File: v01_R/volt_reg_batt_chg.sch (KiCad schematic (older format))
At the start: 13 parts, among them P13 JST-PH2, Q3 PNP, SW3 DIPS_01, U4 MIC5219

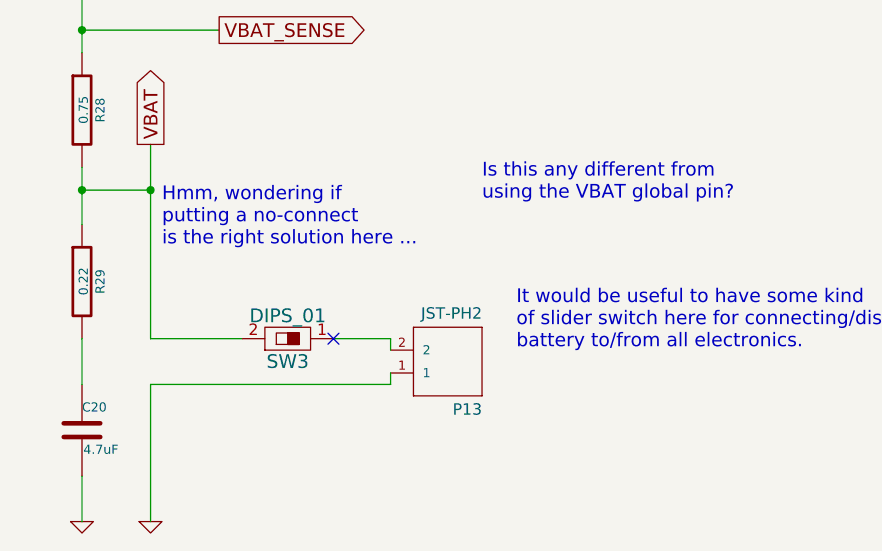
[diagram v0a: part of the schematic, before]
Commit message: Update removes the left channel of the audio circuit.
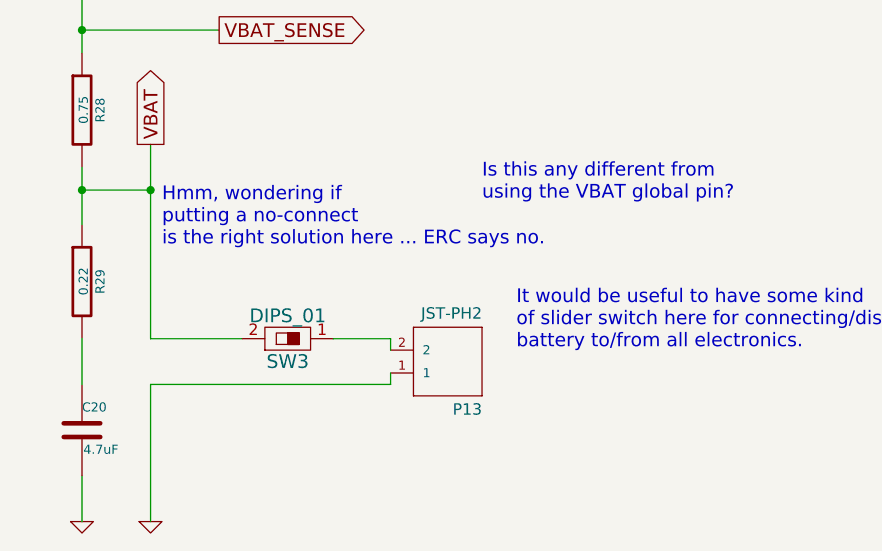
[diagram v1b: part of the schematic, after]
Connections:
- no-connect marks 2 -> 1
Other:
- note added: "Hmm, wondering if \nputting a no-connect\nis the right solution here ... ERC says no."
- note removed: "Hmm, wondering if \nputting a no-connect\nis the right solution here ..."
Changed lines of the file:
@@
 Sheet 4 4
 Title ""
-Date "7 dec 2014"
+Date "16 jan 2015"
 Rev ""
 Comp ""
@@
 $EndComp
 $Comp
-L GND #PWR18
+L GND #PWR013
 U 1 1 5439B1A3
 P 4900 2700
-F 0 "#PWR18" H 4900 2700 30  0001 C CNN
+F 0 "#PWR013" H 4900 2700 30  0001 C CNN
 F 1 "GND" H 4900 2630 30  0001 C CNN
 F 2 "" H 4900 2700 60  0000 C CNN
@@
 $EndComp
 $Comp
-L GND #PWR15
+L GND #PWR014
 U 1 1 5439B578
 P 2250 6250
-F 0 "#PWR15" H 2250 6250 30  0001 C CNN
+F 0 "#PWR014" H 2250 6250 30  0001 C CNN
 F 1 "GND" H 2250 6180 30  0001 C CNN
 F 2 "" H 2250 6250 60  0000 C CNN
@@
 3.3V
 $Comp
-L PWR_FLAG #FLG2
+L PWR_FLAG #FLG015
 U 1 1 5439CBDC
 P 2150 1600
-F 0 "#FLG2" H 2150 1695 30  0001 C CNN
+F 0 "#FLG015" H 2150 1695 30  0001 C CNN
 F 1 "PWR_FLAG" H 2150 1780 30  0000 C CNN
 F 2 "" H 2150 1600 60  0000 C CNN
@@
 $EndComp
 $Comp
-L +BATT #PWR14
+L +BATT #PWR016
 U 1 1 5439CC42
 P 2150 1850
-F 0 "#PWR14" H 2150 1800 20  0001 C CNN
+F 0 "#PWR016" H 2150 1800 20  0001 C CNN
 F 1 "+BATT" H 2150 1950 30  0000 C CNN
 F 2 "" H 2150 1850 60  0000 C CNN
@@
 VIN
 $Comp
-L GND #PWR17
+L GND #PWR017
 U 1 1 5439D063
 P 2550 6250
-F 0 "#PWR17" H 2550 6250 30  0001 C CNN
+F 0 "#PWR017" H 2550 6250 30  0001 C CNN
 F 1 "GND" H 2550 6180 30  0001 C CNN
 F 2 "" H 2550 6250 60  0000 C CNN
@@
 	1850 1600 1850 1850
 $Comp
-L +5V #PWR13
+L +5V #PWR018
 U 1 1 5439CBF7
 P 1850 1850
-F 0 "#PWR13" H 1850 1940 20  0001 C CNN
+F 0 "#PWR018" H 1850 1940 20  0001 C CNN
 F 1 "+5V" H 1850 1940 30  0000 C CNN
 F 2 "" H 1850 1850 60  0000 C CNN
@@
 $EndComp
 $Comp
-L PWR_FLAG #FLG1
+L PWR_FLAG #FLG019
 U 1 1 5439CBEF
 P 1850 1600
-F 0 "#FLG1" H 1850 1695 30  0001 C CNN
+F 0 "#FLG019" H 1850 1695 30  0001 C CNN
 F 1 "PWR_FLAG" H 1850 1780 30  0000 C CNN
 F 2 "" H 1850 1600 60  0000 C CNN
@@
 	2450 1600 2450 1900
 $Comp
-L GND #PWR16
+L GND #PWR020
 U 1 1 5439CC8E
 P 2450 1900
-F 0 "#PWR16" H 2450 1900 30  0001 C CNN
+F 0 "#PWR020" H 2450 1900 30  0001 C CNN
 F 1 "GND" H 2450 1830 30  0001 C CNN
 F 2 "" H 2450 1900 60  0000 C CNN
@@
 $EndComp
 $Comp
-L PWR_FLAG #FLG3
+L PWR_FLAG #FLG021
 U 1 1 5439CBE9
 P 2450 1600
-F 0 "#FLG3" H 2450 1695 30  0001 C CNN
+F 0 "#FLG021" H 2450 1695 30  0001 C CNN
 F 1 "PWR_FLAG" H 2450 1780 30  0000 C CNN
 F 2 "" H 2450 1600 60  0000 C CNN
@@
 	0    -1   -1   0
 $EndComp
-NoConn ~ 3350 5450
 Text Notes 2600 5050 0    60   ~ 0
-Hmm, wondering if \nputting a no-connect\nis the right solution here ...
+Hmm, wondering if \nputting a no-connect\nis the right solution here ... ERC says no.
 $Comp
 L JST-PH2 P13

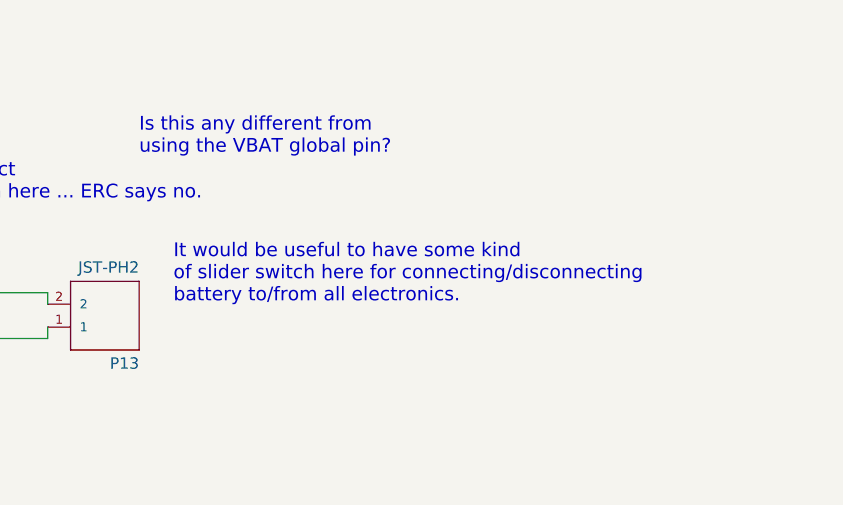
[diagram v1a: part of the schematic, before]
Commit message: Updating entire schematic and footprint selections. Adding jst-ph footprints.
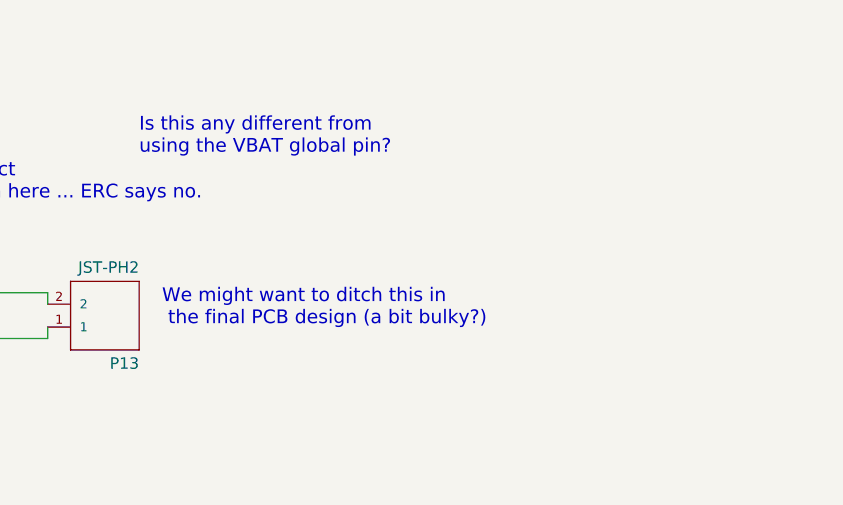
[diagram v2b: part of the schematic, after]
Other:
- note added: "We might want to ditch this in\n the final PCB design (a bit bulky?)"
- note removed: "It would be useful to have some kind \nof slider switch here for connecting/disconnecting \nbattery to/from all electronics."
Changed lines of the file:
@@
 Sheet 4 4
 Title ""
-Date "16 jan 2015"
+Date "17 jan 2015"
 Rev ""
 Comp ""
@@
 $EndComp
 $Comp
-L GND #PWR013
+L GND #PWR012
 U 1 1 5439B1A3
 P 4900 2700
-F 0 "#PWR013" H 4900 2700 30  0001 C CNN
+F 0 "#PWR012" H 4900 2700 30  0001 C CNN
 F 1 "GND" H 4900 2630 30  0001 C CNN
 F 2 "" H 4900 2700 60  0000 C CNN
@@
 $EndComp
 $Comp
-L GND #PWR014
+L GND #PWR013
 U 1 1 5439B578
 P 2250 6250
-F 0 "#PWR014" H 2250 6250 30  0001 C CNN
+F 0 "#PWR013" H 2250 6250 30  0001 C CNN
 F 1 "GND" H 2250 6180 30  0001 C CNN
 F 2 "" H 2250 6250 60  0000 C CNN
@@
 3.3V
 $Comp
-L PWR_FLAG #FLG015
+L PWR_FLAG #FLG014
 U 1 1 5439CBDC
 P 2150 1600
-F 0 "#FLG015" H 2150 1695 30  0001 C CNN
+F 0 "#FLG014" H 2150 1695 30  0001 C CNN
 F 1 "PWR_FLAG" H 2150 1780 30  0000 C CNN
 F 2 "" H 2150 1600 60  0000 C CNN
@@
 $EndComp
 $Comp
-L +BATT #PWR016
+L +BATT #PWR015
 U 1 1 5439CC42
 P 2150 1850
-F 0 "#PWR016" H 2150 1800 20  0001 C CNN
+F 0 "#PWR015" H 2150 1800 20  0001 C CNN
 F 1 "+BATT" H 2150 1950 30  0000 C CNN
 F 2 "" H 2150 1850 60  0000 C CNN
@@
 VIN
 $Comp
-L GND #PWR017
+L GND #PWR016
 U 1 1 5439D063
 P 2550 6250
-F 0 "#PWR017" H 2550 6250 30  0001 C CNN
+F 0 "#PWR016" H 2550 6250 30  0001 C CNN
 F 1 "GND" H 2550 6180 30  0001 C CNN
 F 2 "" H 2550 6250 60  0000 C CNN
@@
 Wire Wire Line
 	1550 3500 1350 3500
-Text Notes 4150 5500 0    60   ~ 0
-It would be useful to have some kind \nof slider switch here for connecting/disconnecting \nbattery to/from all electronics.
+Text Notes 4100 5600 0    60   ~ 0
+We might want to ditch this in\n the final PCB design (a bit bulky?)
 Text Notes 1300 2200 0    60   ~ 0
 I wonder if you need\nthis on all of the sheets ... No.
@@
 	1850 1600 1850 1850
 $Comp
-L +5V #PWR018
+L +5V #PWR017
 U 1 1 5439CBF7
 P 1850 1850
-F 0 "#PWR018" H 1850 1940 20  0001 C CNN
+F 0 "#PWR017" H 1850 1940 20  0001 C CNN
 F 1 "+5V" H 1850 1940 30  0000 C CNN
 F 2 "" H 1850 1850 60  0000 C CNN
@@
 $EndComp
 $Comp
-L PWR_FLAG #FLG019
+L PWR_FLAG #FLG018
 U 1 1 5439CBEF
 P 1850 1600
-F 0 "#FLG019" H 1850 1695 30  0001 C CNN
+F 0 "#FLG018" H 1850 1695 30  0001 C CNN
 F 1 "PWR_FLAG" H 1850 1780 30  0000 C CNN
 F 2 "" H 1850 1600 60  0000 C CNN
@@
 	2450 1600 2450 1900
 $Comp
-L GND #PWR020
+L GND #PWR019
 U 1 1 5439CC8E
 P 2450 1900
-F 0 "#PWR020" H 2450 1900 30  0001 C CNN
+F 0 "#PWR019" H 2450 1900 30  0001 C CNN
 F 1 "GND" H 2450 1830 30  0001 C CNN
 F 2 "" H 2450 1900 60  0000 C CNN
@@
 $EndComp
 $Comp
-L PWR_FLAG #FLG021
+L PWR_FLAG #FLG020
 U 1 1 5439CBE9
 P 2450 1600
-F 0 "#FLG021" H 2450 1695 30  0001 C CNN
+F 0 "#FLG020" H 2450 1695 30  0001 C CNN
 F 1 "PWR_FLAG" H 2450 1780 30  0000 C CNN
 F 2 "" H 2450 1600 60  0000 C CNN

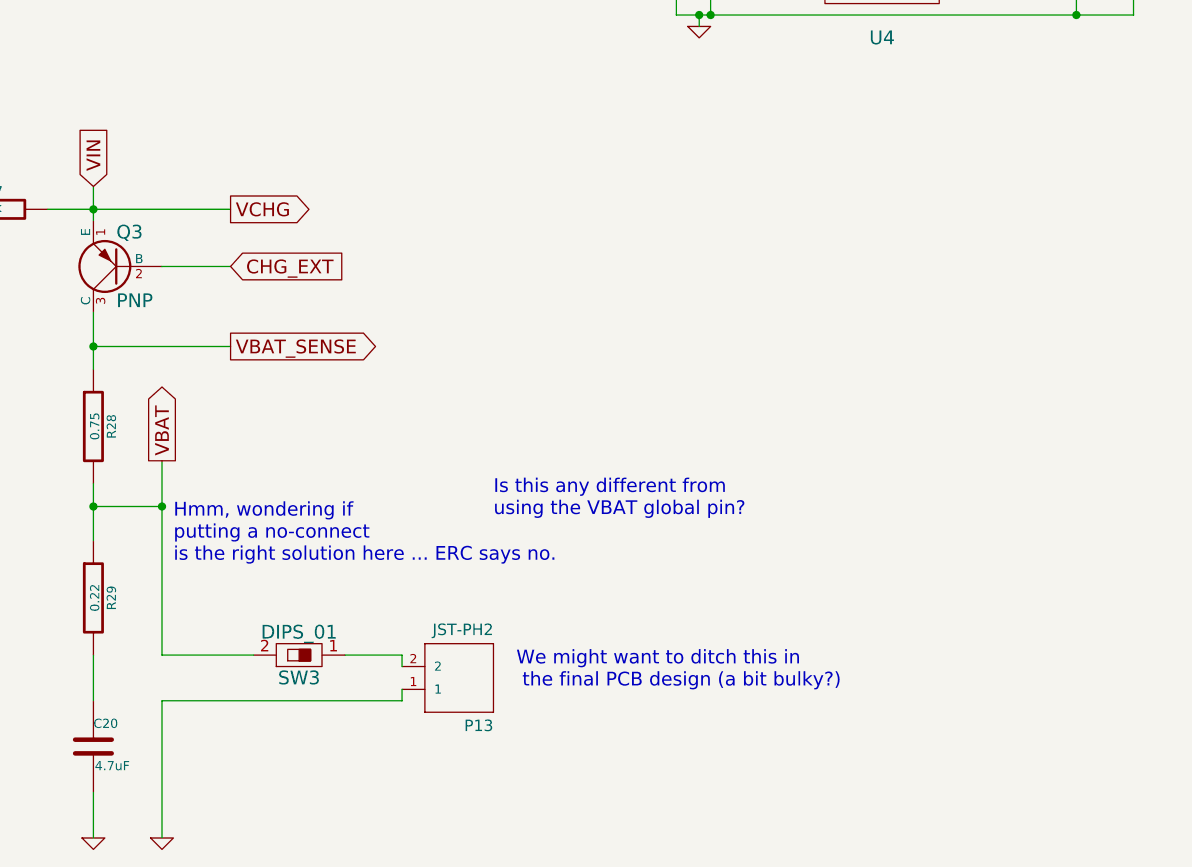
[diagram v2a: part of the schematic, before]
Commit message: Adding very rough initial version of PCB. The BA driver pads were not exact yet (based off of a Sonion driver datasheet).
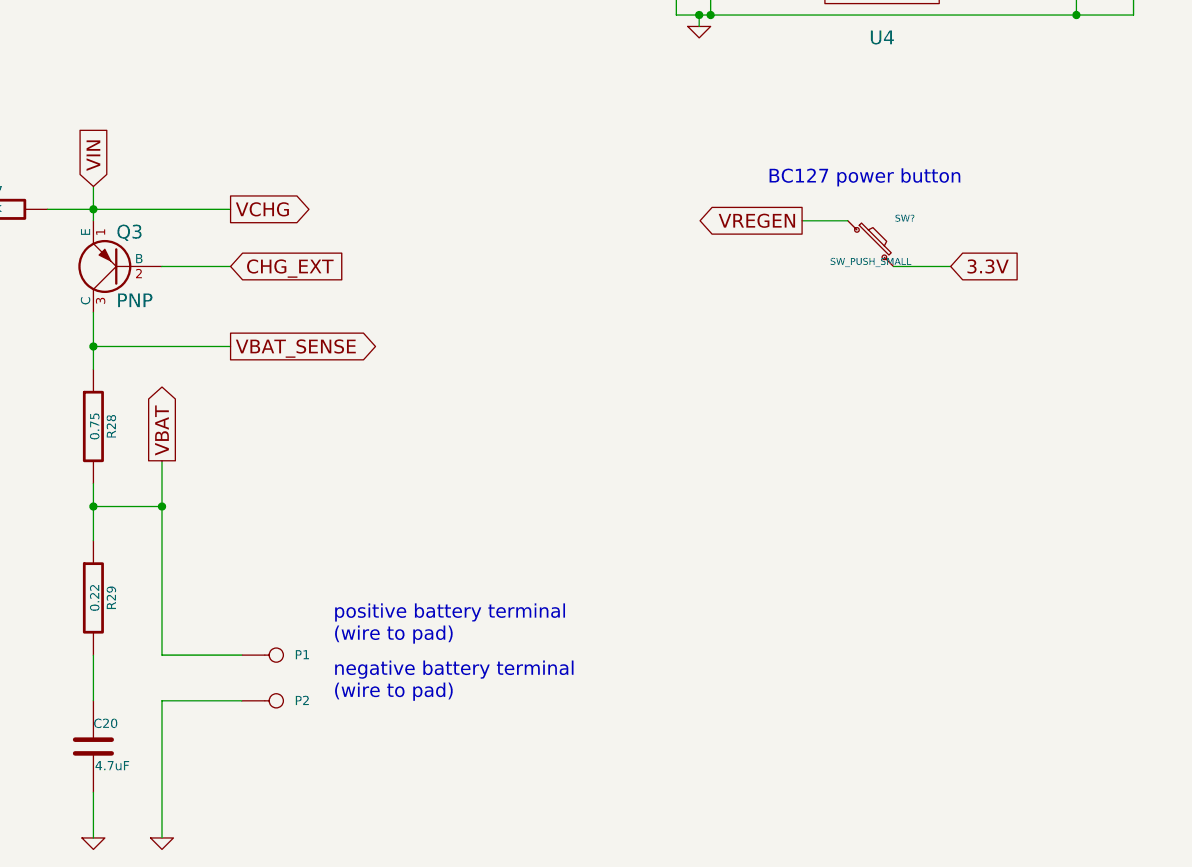
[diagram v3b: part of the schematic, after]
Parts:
- removed P13: JST-PH2, jst-ph-JST-PH2, symbol JST-PH2
- removed SW3: DIPS_01, symbol DIPS_01
- added P1, P2: CONN_1, ~, symbol CONN_1
- added SW?: SW_PUSH_SMALL, ~, symbol SW_PUSH_SMALL
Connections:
- net 3.3V: now also SW?.2
- net GND: now also P2.1
- net VBAT: now also P1.1
- new net VREGEN: SW?.1
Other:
- note added: "BC127 power button"
- note added: "negative battery terminal\n(wire to pad)"
- note added: "positive battery terminal\n(wire to pad)"
- note removed: "Hmm, wondering if \nputting a no-connect\nis the right solution here ... ERC says no."
- note removed: "Is this any different from \nusing the VBAT global pin?"
- note removed: "We might want to ditch this in\n the final PCB design (a bit bulky?)"
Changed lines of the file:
@@
 Sheet 4 4
 Title ""
-Date "17 jan 2015"
+Date "18 jan 2015"
 Rev ""
 Comp ""
@@
 $EndComp
 $Comp
-L GND #PWR012
+L GND #PWR011
 U 1 1 5439B1A3
 P 4900 2700
-F 0 "#PWR012" H 4900 2700 30  0001 C CNN
+F 0 "#PWR011" H 4900 2700 30  0001 C CNN
 F 1 "GND" H 4900 2630 30  0001 C CNN
 F 2 "" H 4900 2700 60  0000 C CNN
@@
 $EndComp
 $Comp
-L GND #PWR013
+L GND #PWR012
 U 1 1 5439B578
 P 2250 6250
-F 0 "#PWR013" H 2250 6250 30  0001 C CNN
+F 0 "#PWR012" H 2250 6250 30  0001 C CNN
 F 1 "GND" H 2250 6180 30  0001 C CNN
 F 2 "" H 2250 6250 60  0000 C CNN
@@
 3.3V
 $Comp
-L PWR_FLAG #FLG014
+L PWR_FLAG #FLG013
 U 1 1 5439CBDC
 P 2150 1600
-F 0 "#FLG014" H 2150 1695 30  0001 C CNN
+F 0 "#FLG013" H 2150 1695 30  0001 C CNN
 F 1 "PWR_FLAG" H 2150 1780 30  0000 C CNN
 F 2 "" H 2150 1600 60  0000 C CNN
@@
 $EndComp
 $Comp
-L +BATT #PWR015
+L +BATT #PWR014
 U 1 1 5439CC42
 P 2150 1850
-F 0 "#PWR015" H 2150 1800 20  0001 C CNN
+F 0 "#PWR014" H 2150 1800 20  0001 C CNN
 F 1 "+BATT" H 2150 1950 30  0000 C CNN
 F 2 "" H 2150 1850 60  0000 C CNN
@@
 VIN
 $Comp
-L GND #PWR016
+L GND #PWR015
 U 1 1 5439D063
 P 2550 6250
-F 0 "#PWR016" H 2550 6250 30  0001 C CNN
+F 0 "#PWR015" H 2550 6250 30  0001 C CNN
 F 1 "GND" H 2550 6180 30  0001 C CNN
 F 2 "" H 2550 6250 60  0000 C CNN
@@
 	2250 3400 2250 3550
 Wire Wire Line
-	3350 5450 3600 5450
+	2550 5450 2900 5450
 Wire Wire Line
 	2550 4600 2550 5450
@@
 Connection ~ 2250 4800
 Wire Wire Line
-	2550 5650 3600 5650
+	2550 5650 2900 5650
 Wire Wire Line
 	2550 5650 2550 6250
@@
 Wire Wire Line
 	1550 3500 1350 3500
-Text Notes 4100 5600 0    60   ~ 0
-We might want to ditch this in\n the final PCB design (a bit bulky?)
 Text Notes 1300 2200 0    60   ~ 0
 I wonder if you need\nthis on all of the sheets ... No.
-Text Notes 4000 4850 0    60   ~ 0
-Is this any different from \nusing the VBAT global pin?
 Wire Wire Line
 	1850 1600 1850 1850
 $Comp
-L +5V #PWR017
+L +5V #PWR016
 U 1 1 5439CBF7
 P 1850 1850
-F 0 "#PWR017" H 1850 1940 20  0001 C CNN
+F 0 "#PWR016" H 1850 1940 20  0001 C CNN
 F 1 "+5V" H 1850 1940 30  0000 C CNN
 F 2 "" H 1850 1850 60  0000 C CNN
@@
 $EndComp
 $Comp
-L PWR_FLAG #FLG018
+L PWR_FLAG #FLG017
 U 1 1 5439CBEF
 P 1850 1600
-F 0 "#FLG018" H 1850 1695 30  0001 C CNN
+F 0 "#FLG017" H 1850 1695 30  0001 C CNN
 F 1 "PWR_FLAG" H 1850 1780 30  0000 C CNN
 F 2 "" H 1850 1600 60  0000 C CNN
@@
 	2450 1600 2450 1900
 $Comp
-L GND #PWR019
+L GND #PWR018
 U 1 1 5439CC8E
 P 2450 1900
-F 0 "#PWR019" H 2450 1900 30  0001 C CNN
+F 0 "#PWR018" H 2450 1900 30  0001 C CNN
 F 1 "GND" H 2450 1830 30  0001 C CNN
 F 2 "" H 2450 1900 60  0000 C CNN
@@
 $EndComp
 $Comp
-L PWR_FLAG #FLG020
+L PWR_FLAG #FLG019
 U 1 1 5439CBE9
 P 2450 1600
-F 0 "#FLG020" H 2450 1695 30  0001 C CNN
+F 0 "#FLG019" H 2450 1695 30  0001 C CNN
 F 1 "PWR_FLAG" H 2450 1780 30  0000 C CNN
 F 2 "" H 2450 1600 60  0000 C CNN
@@
 Wire Wire Line
 	3550 2300 4100 2300
-Wire Wire Line
-	2550 5450 2950 5450
-$Comp
-L DIPS_01 SW3
-U 1 1 544BE30E
-P 3150 5450
-F 0 "SW3" V 3050 5450 60  0000 C CNN
-F 1 "DIPS_01" V 3250 5450 60  0000 C CNN
-F 2 "" H 3150 5450 60  0000 C CNN
-F 3 "" H 3150 5450 60  0000 C CNN
-	1    3150 5450
-	0    -1   -1   0
-$EndComp
-Text Notes 2600 5050 0    60   ~ 0
-Hmm, wondering if \nputting a no-connect\nis the right solution here ... ERC says no.
-$Comp
-L JST-PH2 P13
-U 1 1 5483E1A6
-P 3900 5600
-F 0 "P13" H 3800 5730 50  0000 L BNN
-F 1 "JST-PH2" H 3800 5310 50  0000 L BNN
-F 2 "jst-ph-JST-PH2" H 3900 5750 50  0001 C CNN
-F 3 "" H 3900 5600 60  0000 C CNN
-	1    3900 5600
-	-1   0    0    1
-$EndComp
-Wire Wire Line
-	3600 5650 3600 5600
-Wire Wire Line
-	3600 5450 3600 5500
+$Comp
+L CONN_1 P1
+U 1 1 54BB248C
+P 3050 5450
+F 0 "P1" H 3130 5450 40  0000 L CNN
+F 1 "CONN_1" H 3050 5505 30  0001 C CNN
+F 2 "~" H 3050 5450 60  0000 C CNN
+F 3 "~" H 3050 5450 60  0000 C CNN
+	1    3050 5450
+	1    0    0    -1
+$EndComp
+$Comp
+L CONN_1 P2
+U 1 1 54BB2499
+P 3050 5650
+F 0 "P2" H 3130 5650 40  0000 L CNN
+F 1 "CONN_1" H 3050 5705 30  0001 C CNN
+F 2 "~" H 3050 5650 60  0000 C CNN
+F 3 "~" H 3050 5650 60  0000 C CNN
+	1    3050 5650
+	1    0    0    -1
+$EndComp
+Text Notes 3300 5400 0    60   ~ 0
+positive battery terminal\n(wire to pad)
+Text Notes 3300 5650 0    60   ~ 0
+negative battery terminal\n(wire to pad)
+$Comp
+L SW_PUSH_SMALL SW?
+U 1 1 54BBDE2C
+P 5650 3650
+F 0 "SW?" H 5800 3760 30  0000 C CNN
+F 1 "SW_PUSH_SMALL" H 5650 3571 30  0000 C CNN
+F 2 "~" H 5650 3650 60  0000 C CNN
+F 3 "~" H 5650 3650 60  0000 C CNN
+	1    5650 3650
+	1    0    0    -1
+$EndComp
+Text GLabel 6000 3750 2    60   Input ~ 0
+3.3V
+Wire Wire Line
+	6000 3750 5750 3750
+Text GLabel 5350 3550 0    60   Output ~ 0
+VREGEN
+Wire Wire Line
+	5550 3550 5350 3550
+Text Notes 5200 3400 0    60   ~ 0
+BC127 power button
 $EndSCHEMATC
